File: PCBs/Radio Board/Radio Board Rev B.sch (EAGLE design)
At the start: 2 parts

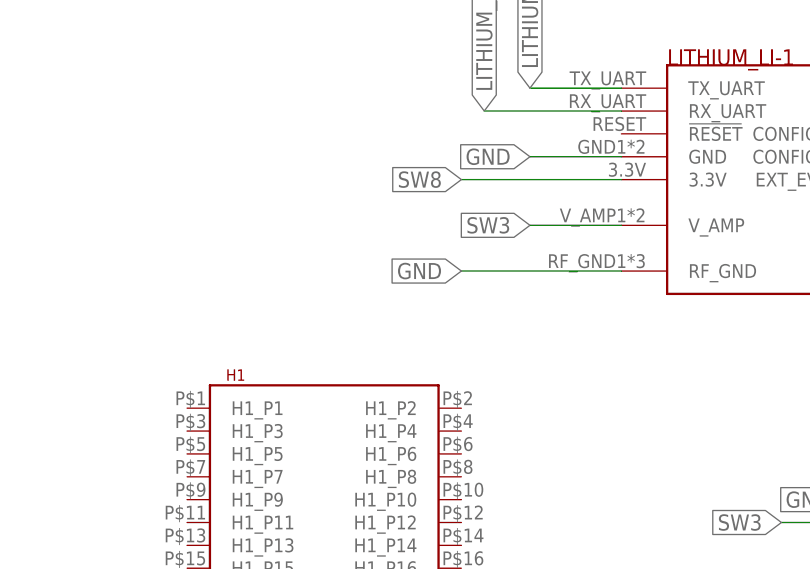
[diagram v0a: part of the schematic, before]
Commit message: Added bypass caps to radio
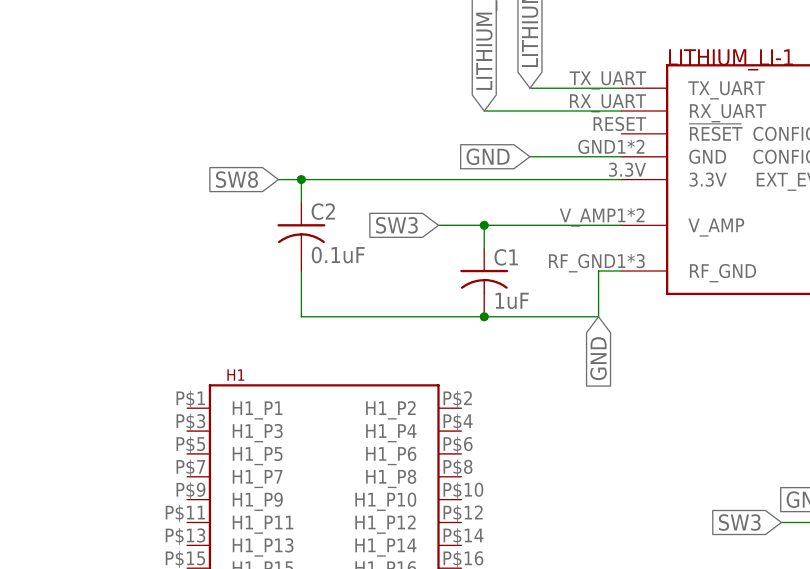
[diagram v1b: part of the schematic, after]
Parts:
- added C1: 1uF, resistor:C-USC0805
- added C2: 0.1uF, resistor:C-USC0805
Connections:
- net GND: now also C1.2, C2.2
- net SW3: now also C1.1
- net SW8: now also C2.1
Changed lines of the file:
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@@
 <part name="U$1" library="Cubesat" deviceset="LITHIUM" device=""/>
 <part name="U$2" library="Cubesat" deviceset="PC104" device=""/>
+<part name="C1" library="resistor" library_urn="urn:adsk.eagle:library:348" deviceset="C-US" device="C0805" package3d_urn="urn:adsk.eagle:package:26137/1" value="1uF"/>
+<part name="C2" library="resistor" library_urn="urn:adsk.eagle:library:348" deviceset="C-US" device="C0805" package3d_urn="urn:adsk.eagle:package:26137/1" value="0.1uF"/>
 </parts>
 <sheets>
@@
 <instance part="U$1" gate="G$1" x="76.2" y="78.74"/>
 <instance part="U$2" gate="G$1" x="25.4" y="0"/>
+<instance part="C1" gate="G$1" x="55.88" y="81.28"/>
+<instance part="C2" gate="G$1" x="35.56" y="86.36"/>
 </instances>
 <busses>
@@
 <wire x1="71.12" y1="93.98" x2="60.96" y2="93.98" width="0.1524" layer="91"/>
 <label x="60.96" y="93.98" size="1.778" layer="95" rot="R180" xref="yes"/>
-</segment>
-<segment>
-<pinref part="U$1" gate="G$1" pin="RF_GND"/>
-<wire x1="71.12" y1="81.28" x2="53.34" y2="81.28" width="0.1524" layer="91"/>
-<label x="53.34" y="81.28" size="1.778" layer="95" rot="R180" xref="yes"/>
 </segment>
 <segment>
@@
 <label x="134.62" y="7.62" size="1.778" layer="95" xref="yes"/>
 </segment>
+<segment>
+<pinref part="C2" gate="G$1" pin="2"/>
+<wire x1="35.56" y1="81.28" x2="35.56" y2="76.2" width="0.1524" layer="91"/>
+<pinref part="C1" gate="G$1" pin="2"/>
+<wire x1="35.56" y1="76.2" x2="55.88" y2="76.2" width="0.1524" layer="91"/>
+<wire x1="55.88" y1="76.2" x2="68.58" y2="76.2" width="0.1524" layer="91"/>
+<junction x="55.88" y="76.2"/>
+<wire x1="68.58" y1="76.2" x2="68.58" y2="81.28" width="0.1524" layer="91"/>
+<pinref part="U$1" gate="G$1" pin="RF_GND"/>
+<wire x1="68.58" y1="81.28" x2="71.12" y2="81.28" width="0.1524" layer="91"/>
+<label x="68.58" y="76.2" size="1.778" layer="95" rot="R270" xref="yes"/>
+</segment>
 </net>
 <net name="SW3" class="0">
@@
 <segment>
 <pinref part="U$1" gate="G$1" pin="V_AMP"/>
-<wire x1="71.12" y1="86.36" x2="60.96" y2="86.36" width="0.1524" layer="91"/>
-<label x="60.96" y="86.36" size="1.778" layer="95" rot="R180" xref="yes"/>
+<wire x1="71.12" y1="86.36" x2="55.88" y2="86.36" width="0.1524" layer="91"/>
+<label x="50.8" y="86.36" size="1.778" layer="95" rot="R180" xref="yes"/>
+<pinref part="C1" gate="G$1" pin="1"/>
+<wire x1="55.88" y1="86.36" x2="50.8" y2="86.36" width="0.1524" layer="91"/>
+<wire x1="55.88" y1="86.36" x2="55.88" y2="83.82" width="0.1524" layer="91"/>
+<junction x="55.88" y="86.36"/>
 </segment>
 </net>
@@
 <segment>
 <pinref part="U$1" gate="G$1" pin="3.3V"/>
-<wire x1="71.12" y1="91.44" x2="53.34" y2="91.44" width="0.1524" layer="91"/>
-<label x="53.34" y="91.44" size="1.778" layer="95" rot="R180" xref="yes"/>
+<wire x1="71.12" y1="91.44" x2="35.56" y2="91.44" width="0.1524" layer="91"/>
+<label x="33.02" y="91.44" size="1.778" layer="95" rot="R180" xref="yes"/>
+<pinref part="C2" gate="G$1" pin="1"/>
+<wire x1="35.56" y1="91.44" x2="33.02" y2="91.44" width="0.1524" layer="91"/>
+<wire x1="35.56" y1="91.44" x2="35.56" y2="88.9" width="0.1524" layer="91"/>
+<junction x="35.56" y="91.44"/>
 </segment>
 </net>
@@
 </schematic>
 </drawing>
+<compatibility>
+<note version="8.2" severity="warning">
+Since Version 8.2, EAGLE supports online libraries. The ids
+of those online libraries will not be understood (or retained)
+with this version.
+</note>
+<note version="8.3" severity="warning">
+Since Version 8.3, EAGLE supports URNs for individual library
+assets (packages, symbols, and devices). The URNs of those assets
+will not be understood (or retained) with this version.
+</note>
+<note version="8.3" severity="warning">
+Since Version 8.3, EAGLE supports the association of 3D packages
+with devices in libraries, schematics, and board files. Those 3D
+packages will not be understood (or retained) with this version.
+</note>
+</compatibility>
 </eagle>

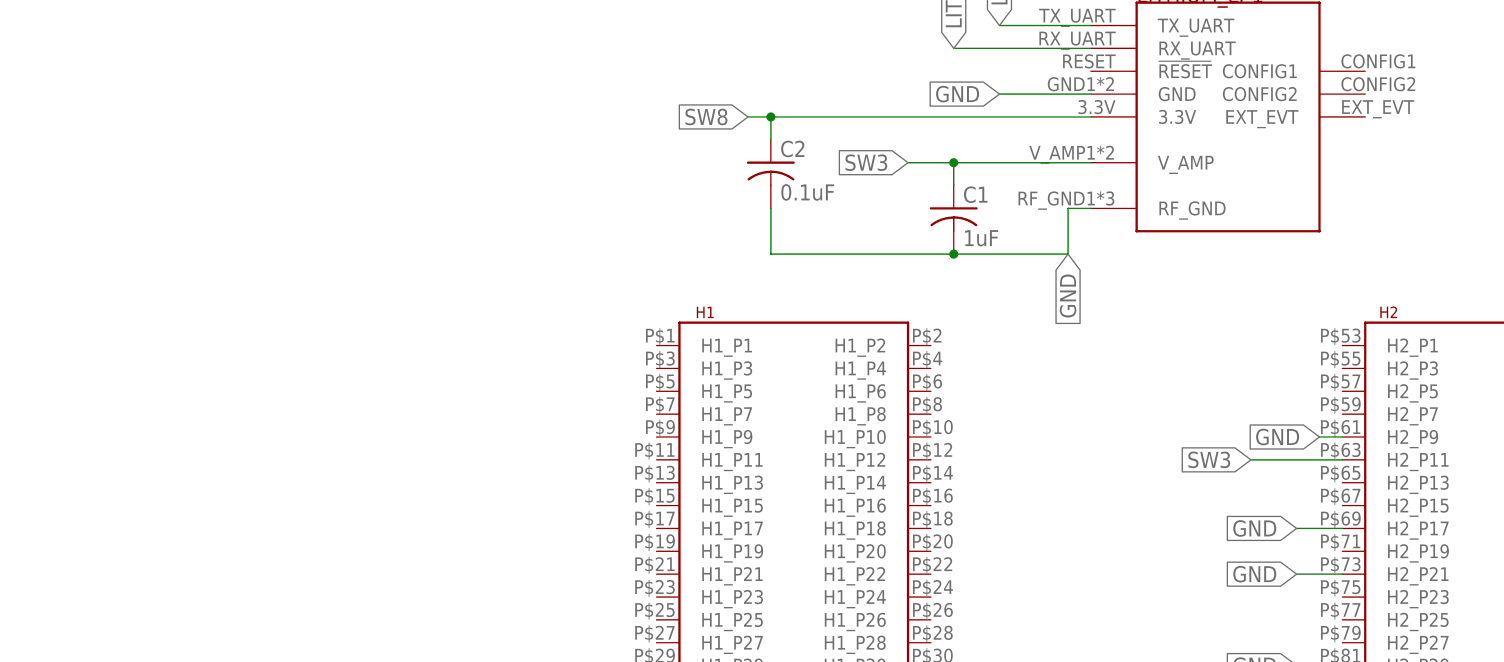
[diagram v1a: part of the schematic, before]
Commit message: Add temp sensors to GPS and Radio boards
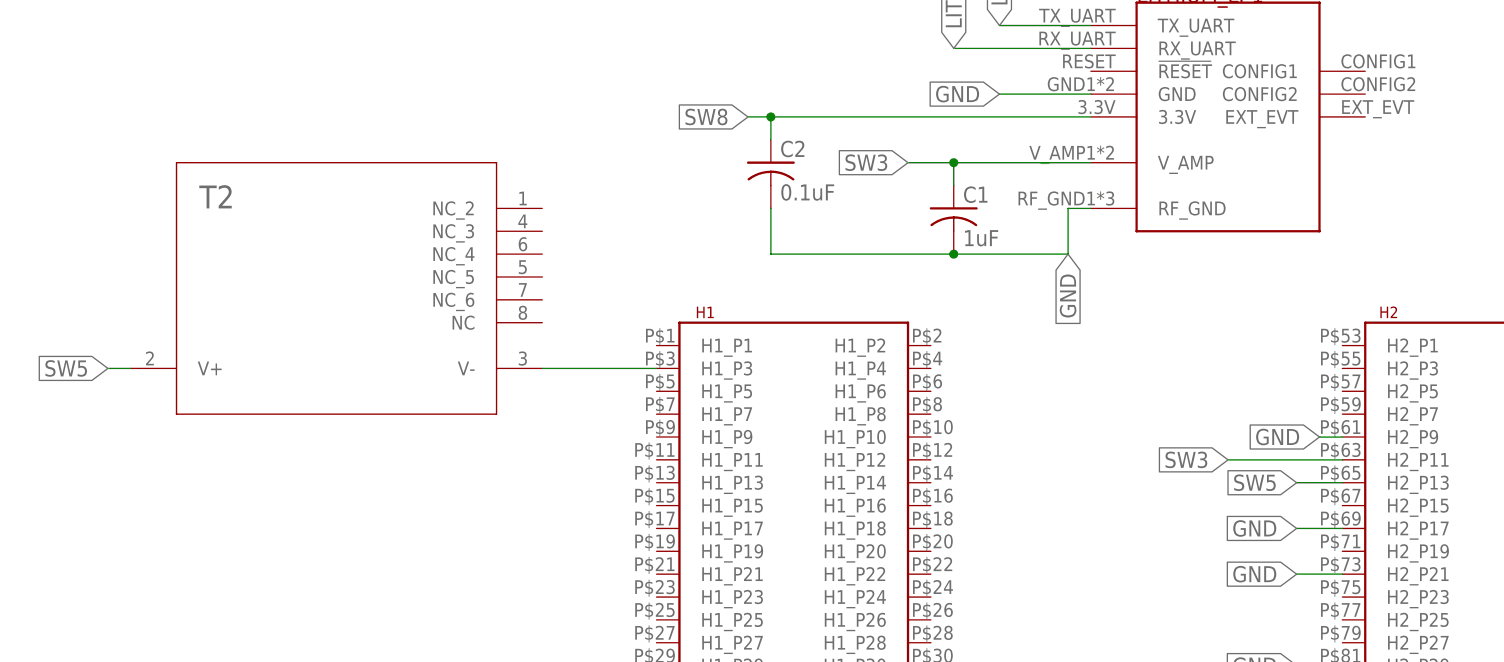
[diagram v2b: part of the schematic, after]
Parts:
- added T2: AD590KRZ, AD590KRZ:AD590KRZ
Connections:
- new net N$1: T2.V-, U$2.H1_P3
- new net SW5: T2.V+, U$2.H2_P13
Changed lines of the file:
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@@
 <layer number="57" name="tCAD" color="7" fill="1" visible="no" active="no"/>
 <layer number="58" name="bCAD" color="7" fill="1" visible="no" active="no"/>
+<layer number="88" name="SimResults" color="9" fill="1" visible="yes" active="yes"/>
+<layer number="89" name="SimProbes" color="9" fill="1" visible="yes" active="yes"/>
 <layer number="90" name="Modules" color="5" fill="1" visible="yes" active="yes"/>
 <layer number="91" name="Nets" color="2" fill="1" visible="yes" active="yes"/>
@@
 <part name="C1" library="resistor" library_urn="urn:adsk.eagle:library:348" deviceset="C-US" device="C0805" package3d_urn="urn:adsk.eagle:package:26137/1" value="1uF"/>
 <part name="C2" library="resistor" library_urn="urn:adsk.eagle:library:348" deviceset="C-US" device="C0805" package3d_urn="urn:adsk.eagle:package:26137/1" value="0.1uF"/>
+<part name="T2" library="AD590KRZ" deviceset="AD590KRZ" device=""/>
 </parts>
 <sheets>
@@
 <instance part="C1" gate="G$1" x="55.88" y="81.28"/>
 <instance part="C2" gate="G$1" x="35.56" y="86.36"/>
+<instance part="T2" gate="A" x="-30.48" y="58.42"/>
 </instances>
 <busses>
@@
 <segment>
 <pinref part="U$2" gate="G$1" pin="H2_P11"/>
-<wire x1="99.06" y1="53.34" x2="88.9" y2="53.34" width="0.1524" layer="91"/>
-<label x="88.9" y="53.34" size="1.778" layer="95" rot="R180" xref="yes"/>
+<wire x1="99.06" y1="53.34" x2="86.36" y2="53.34" width="0.1524" layer="91"/>
+<label x="86.36" y="53.34" size="1.778" layer="95" rot="R180" xref="yes"/>
 </segment>
 <segment>
@@
 </segment>
 </net>
+<net name="SW5" class="0">
+<segment>
+<pinref part="U$2" gate="G$1" pin="H2_P13"/>
+<wire x1="99.06" y1="50.8" x2="93.98" y2="50.8" width="0.1524" layer="91"/>
+<label x="93.98" y="50.8" size="1.778" layer="95" rot="R180" xref="yes"/>
+</segment>
+<segment>
+<pinref part="T2" gate="A" pin="V+"/>
+<wire x1="-35.56" y1="63.5" x2="-38.1" y2="63.5" width="0.1524" layer="91"/>
+<label x="-38.1" y="63.5" size="1.778" layer="95" rot="R180" xref="yes"/>
+</segment>
+</net>
+<net name="N$1" class="0">
+<segment>
+<pinref part="T2" gate="A" pin="V-"/>
+<pinref part="U$2" gate="G$1" pin="H1_P3"/>
+<wire x1="10.16" y1="63.5" x2="22.86" y2="63.5" width="0.1524" layer="91"/>
+</segment>
+</net>

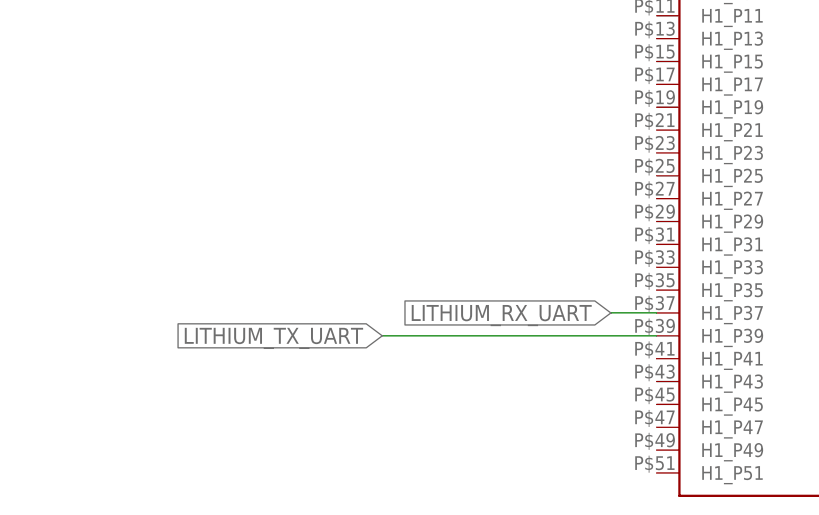
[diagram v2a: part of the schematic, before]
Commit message: Changed Li Tx/Rx pins
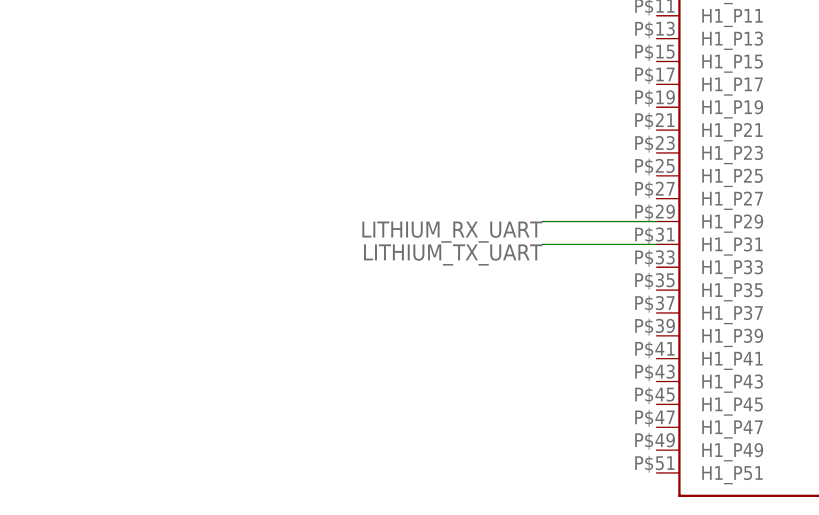
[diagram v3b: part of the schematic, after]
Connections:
- net LITHIUM_RX_UART: now also U$2.H1_P29; no longer U$2.H1_P37
- net LITHIUM_TX_UART: now also U$2.H1_P31; no longer U$2.H1_P39
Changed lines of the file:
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@@
 <?xml version="1.0" encoding="utf-8"?>
 <!DOCTYPE eagle SYSTEM "eagle.dtd">
-<eagle version="9.0.1">
+<eagle version="9.1.0">
 <drawing>
 <settings>
@@
 </segment>
 <segment>
-<pinref part="U$2" gate="G$1" pin="H1_P39"/>
-<wire x1="22.86" y1="17.78" x2="-7.62" y2="17.78" width="0.1524" layer="91"/>
-<label x="-7.62" y="17.78" size="1.778" layer="95" rot="R180" xref="yes"/>
+<pinref part="U$2" gate="G$1" pin="H1_P31"/>
+<wire x1="22.86" y1="27.94" x2="10.16" y2="27.94" width="0.1524" layer="91"/>
+<label x="10.16" y="27.94" size="1.778" layer="95" rot="R180"/>
 </segment>
 </net>
@@
 </segment>
 <segment>
-<pinref part="U$2" gate="G$1" pin="H1_P37"/>
-<wire x1="22.86" y1="20.32" x2="17.78" y2="20.32" width="0.1524" layer="91"/>
-<label x="17.78" y="20.32" size="1.778" layer="95" rot="R180" xref="yes"/>
-</segment>
-</net>
+<pinref part="U$2" gate="G$1" pin="H1_P29"/>
+<wire x1="22.86" y1="30.48" x2="10.16" y2="30.48" width="0.1524" layer="91"/>
+<label x="10.16" y="30.48" size="1.778" layer="95" rot="R180"/>
+</segment>
+</net>
